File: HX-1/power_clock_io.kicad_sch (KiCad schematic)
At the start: 30 parts, among them J2 Conn_01x02_Socket, J5 3V3_Out, J6 5V_Out, U3 XC6206P332MR-G, Y1 16MHz

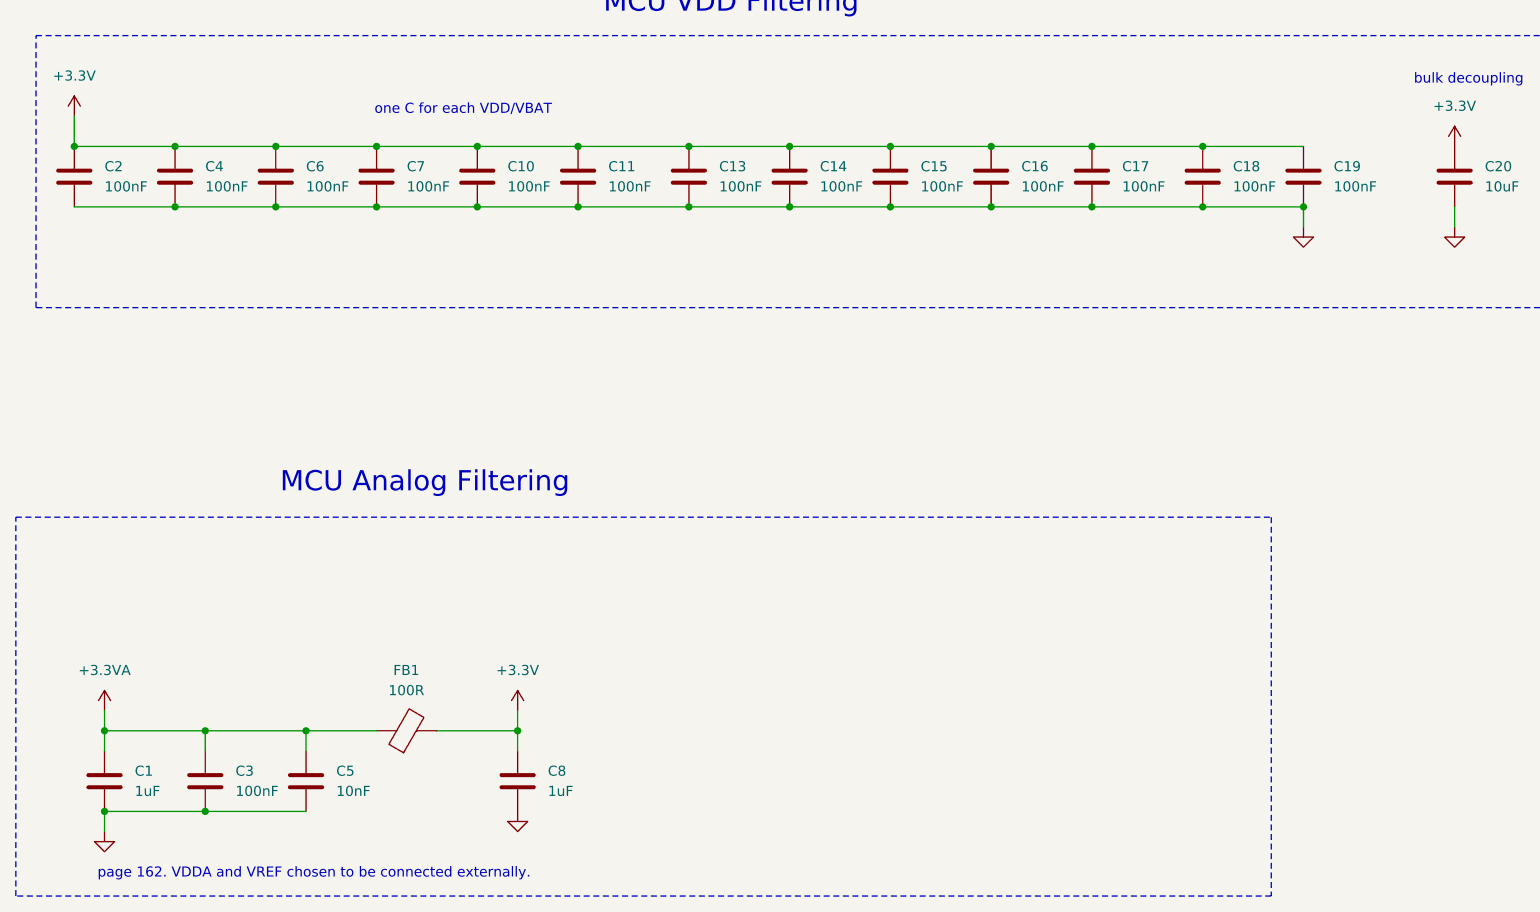
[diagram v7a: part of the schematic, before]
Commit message: change most passive components to 0402 to save space
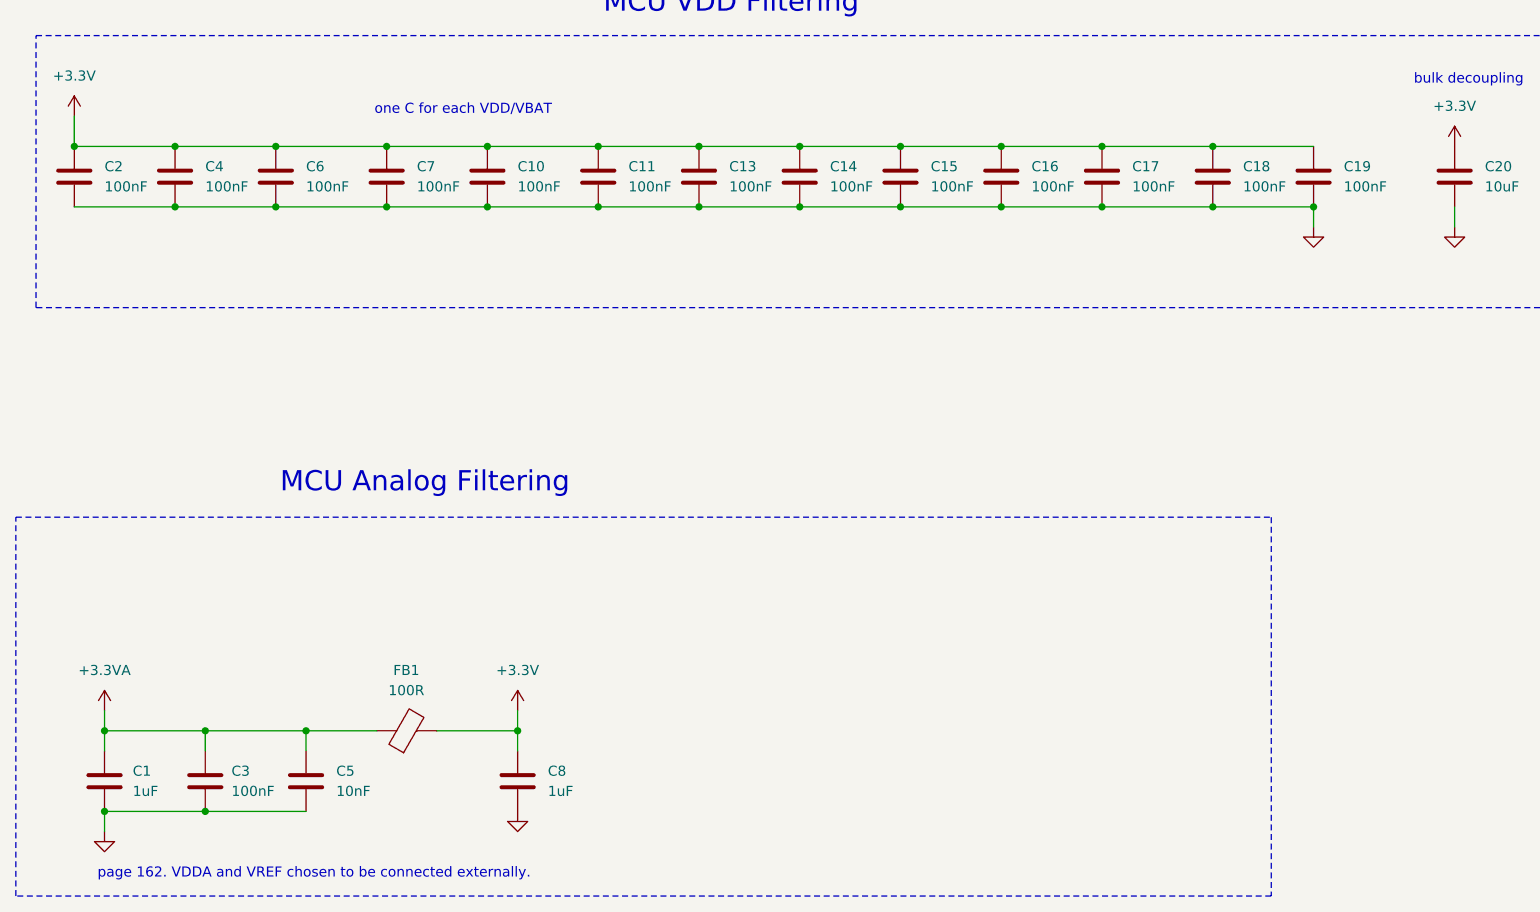
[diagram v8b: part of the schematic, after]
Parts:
- C1, C25, C26, C8: footprint Capacitor_SMD:C_0603_1608Metric -> Capacitor_SMD:C_0402_1005Metric; LCSC PN C15849 -> C52923
- C10, C11, C13, C14, C15, C16, C17, C18, C19, C2, C3, C4, C6, C7: footprint Capacitor_SMD:C_0603_1608Metric -> Capacitor_SMD:C_0402_1005Metric; LCSC PN C14663 -> C1525
